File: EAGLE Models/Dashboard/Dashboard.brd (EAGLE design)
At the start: 127 x 81.3 mm, 86 parts, among them IC1 AT90CAN128, IC2 MCP2551SO8, IC3 NUP2105L, IC5 FT232RL, Q1 56P2859, U1 74LCX125M

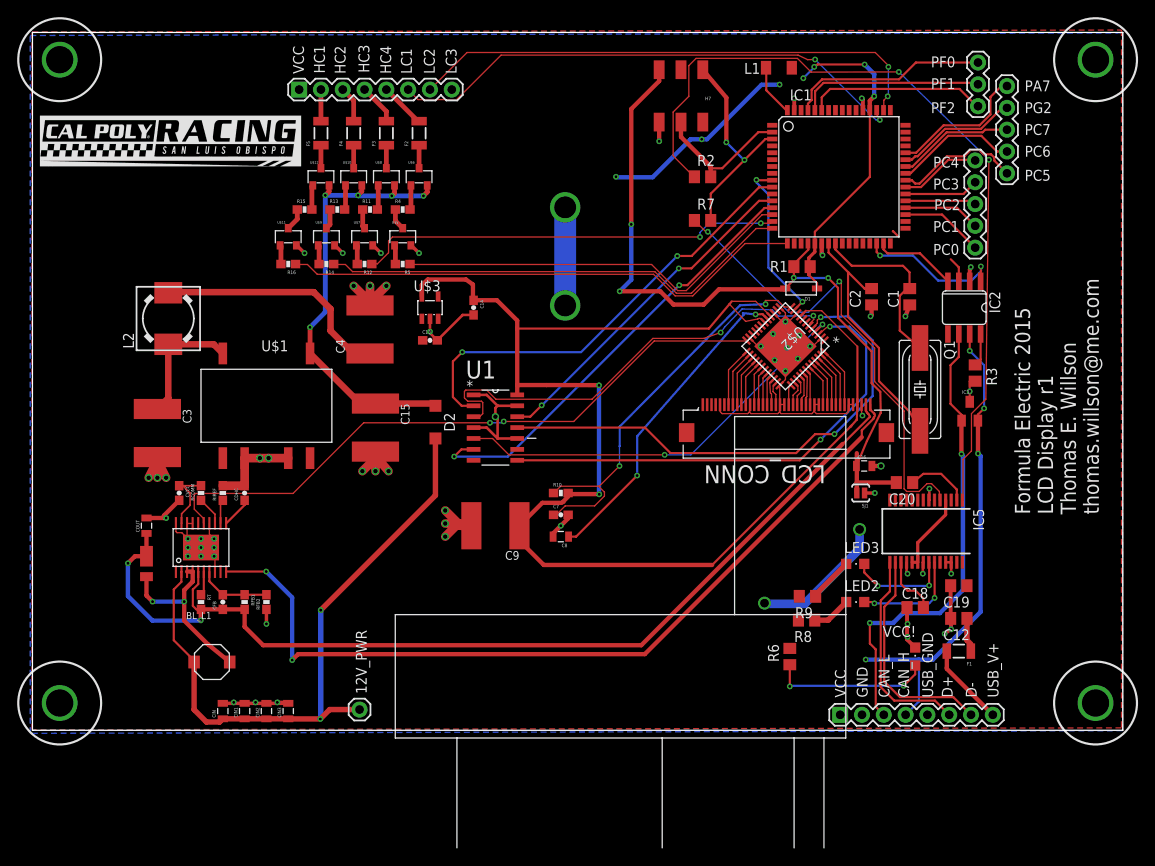
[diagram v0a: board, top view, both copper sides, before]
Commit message: Merge Combustion EAGLE documents and cleanup some of the repo.
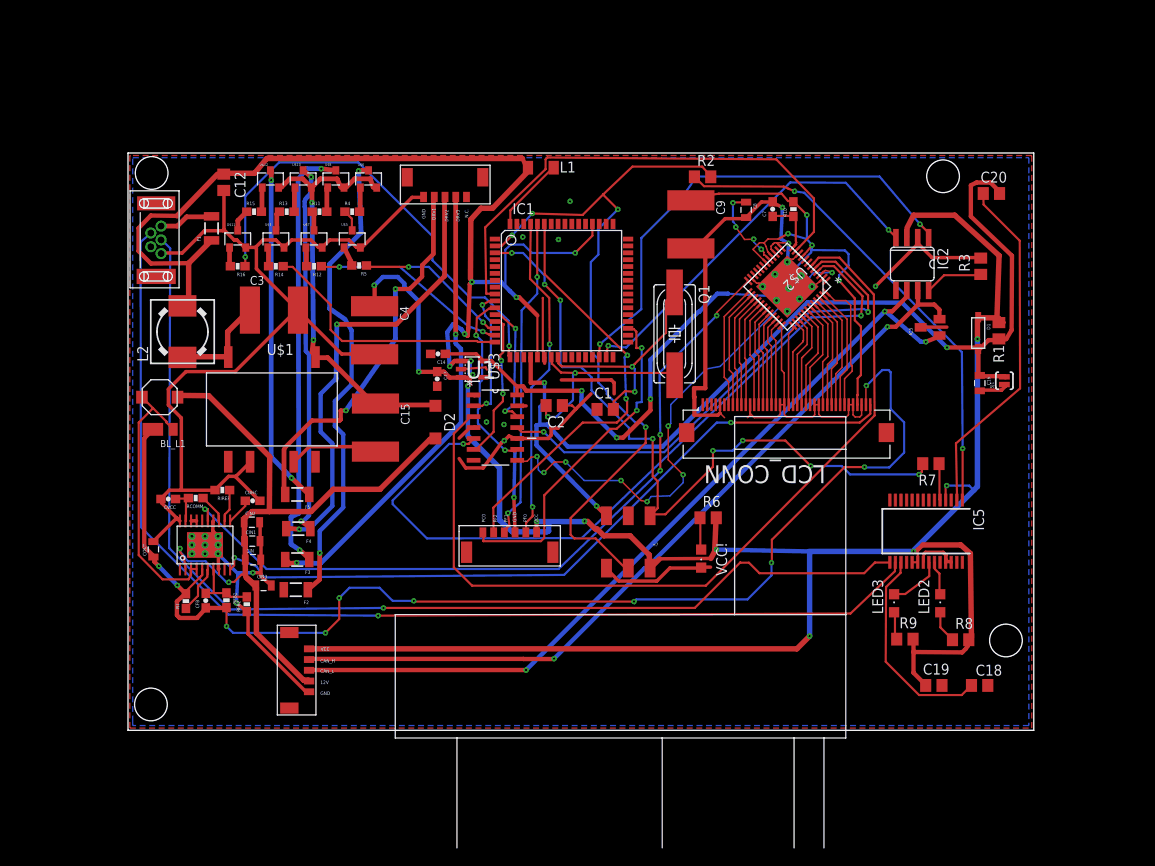
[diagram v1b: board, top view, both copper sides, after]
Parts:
- removed 12V_PWR: M01PTH, SparkFun-Connectors:1X01
- removed CAN_UC_CONN, DRIVER_OUTPUTS: (no value), SparkFun-Connectors:1X08
- removed DRIVER_INPUTS_1, DRIVER_INPUTS_3: (no value), SparkFun-Connectors:1X05
- removed DRIVER_INPUTS_2: (no value), SparkFun-Connectors:1X03
- added CANPWR, LEDOUT: MICRO5LOCK, DashAndCAN library:MICRO5LOCK
- added ROT/PUSH: MICRO6LOCK, DashAndCAN library:MICRO6LOCK
- added U$14: MUSBB, DashAndCAN library:MUSBB
- moved F1 100.0 mm to (8.16, 58.5), turned to 90 degrees
- moved C12 99.6 mm to (9.58, 63.8), turned to 270 degrees
- moved F2 55.1 mm to (18.0, 16.4), turned to 180 degrees
- moved H7 52.3 mm to (56.7, 21.9)
- moved F3 50.7 mm to (18.1, 19.9), turned to 180 degrees
- moved F4 46.5 mm to (18.3, 23.5), turned to 180 degrees
- moved C8 43.8 mm to (70.4, 60.6), turned to 270 degrees
- moved C7 43.3 mm to (73.5, 60.7), turned to 90 degrees
- moved R10 42.7 mm to (75.9, 60.7), turned to 90 degrees
- moved F5 42.2 mm to (18.1, 27.5), turned to 180 degrees
- moved C9 41.8 mm to (64.0, 58.9), turned to 270 degrees
- moved C2 39.1 mm to (48.1, 37.8), turned to 180 degrees
- moved R7 38.9 mm to (91.9, 31.1), turned to 180 degrees
- moved C1 37.8 mm to (54.0, 37.4), turned to 0 degrees
- moved C20 35.2 mm to (99.0, 62.5), turned to 0 degrees
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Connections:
- removed net AVR_SCK: IC1.11
- removed net PC1: DRIVER_INPUTS_1.2, IC1.36
- removed net PC2: DRIVER_INPUTS_1.3, IC1.37
- removed net PC3: DRIVER_INPUTS_1.4, IC1.38
- removed net PC5: DRIVER_INPUTS_3.5, IC1.40
- removed net PC6: DRIVER_INPUTS_3.4, IC1.41
- removed net PC7: DRIVER_INPUTS_3.3, IC1.42
- removed net PG2: DRIVER_INPUTS_3.2, IC1.43
- net 12V: now also CANPWR.P2; no longer 12V_PWR.1
- net AVR_SCLK: now also IC1.11
- net CAN_H: now also CANPWR.P4; no longer CAN_UC_CONN.4
- net CAN_L: now also CANPWR.P3; no longer CAN_UC_CONN.3
- net D+: now also U$14.P3; no longer CAN_UC_CONN.6
- net D-: now also U$14.P2; no longer CAN_UC_CONN.7
- net DRV1: now also LEDOUT.P2; no longer DRIVER_OUTPUTS.2
- net DRV2: now also LEDOUT.P3; no longer DRIVER_OUTPUTS.3
- net DRV3: now also LEDOUT.P4; no longer DRIVER_OUTPUTS.4
- net DRV4: no longer DRIVER_OUTPUTS.5
- net GND: now also CANPWR.P1, LEDOUT.P1, ROT/PUSH.P4, U$14.P5; no longer CAN_UC_CONN.2, CAN_UC_CONN.5, DRIVER_OUTPUTS.8
- net PA0: no longer DRIVER_OUTPUTS.6
- net PA1: no longer DRIVER_OUTPUTS.7
- net PA7: no longer DRIVER_INPUTS_3.1
- net PC0: now also ROT/PUSH.P1; no longer DRIVER_INPUTS_1.1
- net PC4: no longer DRIVER_INPUTS_1.5
- net PF0: now also ROT/PUSH.P5; no longer DRIVER_INPUTS_2.1
- net PF1: now also ROT/PUSH.P3; no longer DRIVER_INPUTS_2.2
- net PF2: now also ROT/PUSH.P2; no longer DRIVER_INPUTS_2.3
- net USB_V_IN: now also U$14.P1; no longer CAN_UC_CONN.8
- net VCC: now also CANPWR.P5, ROT/PUSH.P6; no longer CAN_UC_CONN.1, DRIVER_OUTPUTS.1
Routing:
- net VCC: track 135.2 -> 402.3 mm, vias 11 -> 17
- net GND: track 172.8 -> 394.9 mm, vias 49 -> 12
- net D-: track 26.1 -> 129.9 mm, vias 0 -> 1
- net D+: track 24.3 -> 126.5 mm, vias 0 -> 1
- net RX: track 16.7 -> 86.2 mm, vias 0 -> 4
- net PA0: track 61.9 -> 0.00 mm, vias 2 -> 0
- net PA1: track 61.2 -> 0.00 mm, vias 2 -> 0
- net TX: track 25.3 -> 82.8 mm, vias 2 -> 8
- net N$26: track 2.68 -> 55.6 mm, vias 0 -> 2
- net M8TXD: track 56.1 -> 4.29 mm, vias 2 -> 0
- net DRV3: track 4.73 -> 54.0 mm, vias 0 -> 2
- net DRV2: track 4.21 -> 53.3 mm, vias 0 -> 2
- net N$30: track 2.68 -> 50.9 mm, vias 0 -> 2
- net FT801_CS_N: track 53.4 -> 100.5 mm, vias 2 -> 0
- net 3.3V: track 161.7 -> 117.7 mm, vias 2 -> 7
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- added copper zone on layer 1, net GND
- removed copper zone on layer 1, net VCC
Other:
- board size 127 x 81.3 mm -> 105.5 x 67.2 mm
- board text added: "12V"
- board text added: "DRV1"
- board text added: "DRV2"
- board text added: "DRV3"
- board text added: "Formula SAE 2016 LCD Display r2"
- board text added: "N.C."
- board text removed: "D+"
- board text removed: "D-"
- board text removed: "Formula Electric 2015 LCD Display r1 Thomas E. Willson thomas.willson@me.com"
- board text removed: "HC1"
- board text removed: "HC2"
- board text removed: "HC3"
- board text removed: "HC4"
- board text removed: "LC1"
- board text removed: "LC2"
- board text removed: "LC3"
- board text removed: "PA7"
- board text removed: "PC1"
- board text removed: "PC2"
- board text removed: "PC3"
- board text removed: "PC4"
- board text removed: "PC5"
- board text removed: "PC6"
- board text removed: "PC7"
- board text removed: "PG2"
- board text removed: "USB_GND"
- board text removed: "USB_V+"
